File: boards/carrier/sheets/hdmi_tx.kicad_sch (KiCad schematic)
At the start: 14 parts, among them J1 HDMI-019S, U1 TPD12S016PWR, U2 24LC256T-I/SN

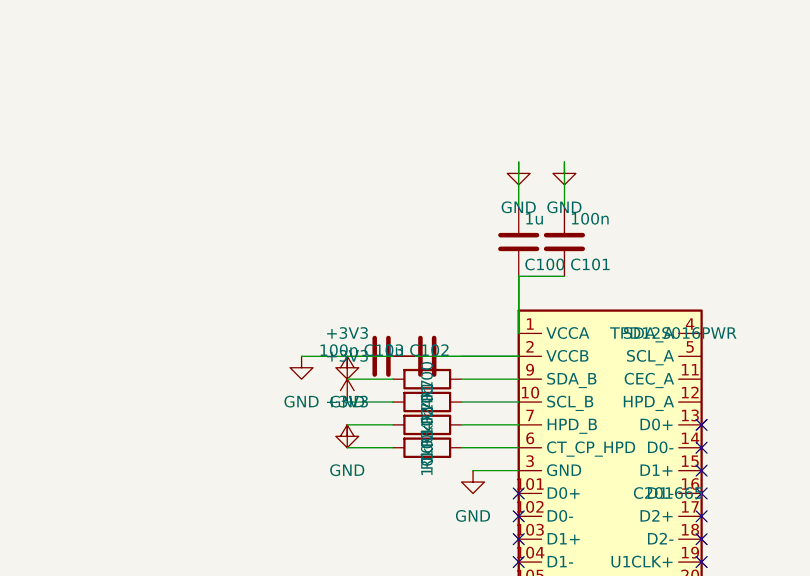
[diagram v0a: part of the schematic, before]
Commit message: Stage 5.5: rotation-derived pin sides + per-edge slot pitch (cluster fix)
Applies the in-flight cluster-fix agent's work (session limit cut its
own commit short). Two architectural changes that close the
sub-sheet wire_dangling / net-merging class of errors:

1) Rotation-derived page-side detection
   (core/layout/geometry.py + core/layout/cluster.py)

   Previously cluster.pin_side() compared abs(pin.x) vs abs(pin.y) on
   the symbol-relative coordinate to guess which body edge a pin
   emerges from. This mis-classified pins on ICs whose pin columns
   span a larger y-range than the body width — FUSB302's seven
   left-column pins (±7.62 mm in y) on a 20 mm-wide body wrap to
   "top/bottom" with the axis-dominance rule, but they're actually
   left-edge pins. The cluster then places passives on the wrong
   side and the resulting wires collide into other nets.

   The new page_side_from_pin() helper derives the page-side from the
   pin's intrinsic KiCad rotation (0 = LEFT edge, 90 = BOTTOM, 180 =
   RIGHT, 270 = TOP) combined with the placed symbol's rotation. This
   is the canonical KiCad convention and doesn't depend on body
   proportions.

   PinGeometry / PinGeometryAbs gain pin_rotation + symbol_rotation
   fields; SymbolGeometryCache reads pin.rotation from the cached
   SymbolDefinition (kicad-sch-api's list_pins() flattens it away).
   pin_side() takes optional pin_rotation/symbol_rotation; falls back
   to the legacy heuristic when not supplied.

2) Per-edge slot pitch
   (core/layout/_constants.py + core/layout/cluster.py)

   LEFT/RIGHT-edge passive swarms fan OUTWARD along the perpendicular
   axis: each slot is one passive body + one power-symbol stub further
   out. The pitch must clear 2 × PASSIVE_PIN_HALF (7.62 mm) +
   POWER_SYMBOL_OFFSET (5.08 mm), so HORIZONTAL_SWARM_PITCH_MM is now
   15.24 mm — was previously the same 5.08 mm used for TOP/BOTTOM, so
   adjacent slots' endpoints collapsed onto one another and KiCad
   merged the entire stack 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
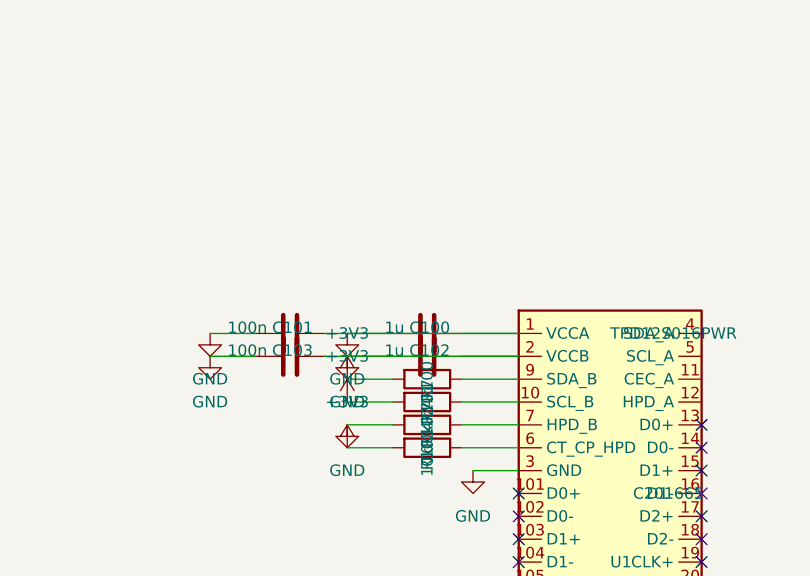
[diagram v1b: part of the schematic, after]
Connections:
- net +5V: now also C100.2, C101.2, C102.1, C103.1, U1.1 (VCCA), U1.2 (VCCB)
